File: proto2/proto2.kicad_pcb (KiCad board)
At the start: 2 copper layers, 187.5 x 109.8 mm, 182 parts, among them J1 Output 1, J10 Output, J11 Device, J12 Daughter Card, J2 Main Power, J3 Output, J4 Output, J5 Device, J6 Output, J7 Device, J8 Output, J9 Device, SW1 SW_DIP_x04, U1 AQY282SX, U10 AQY282SX, U11 AQY282SX, U12 AQY282SX, U13 LDO, U2 AQY282SX, U3 AQY282SX, U4 AQY282SX, U5 AQY282SX, U6 AQY282SX, U7 AQY282SX, U8 AQY282SX, U9 AQY282SX

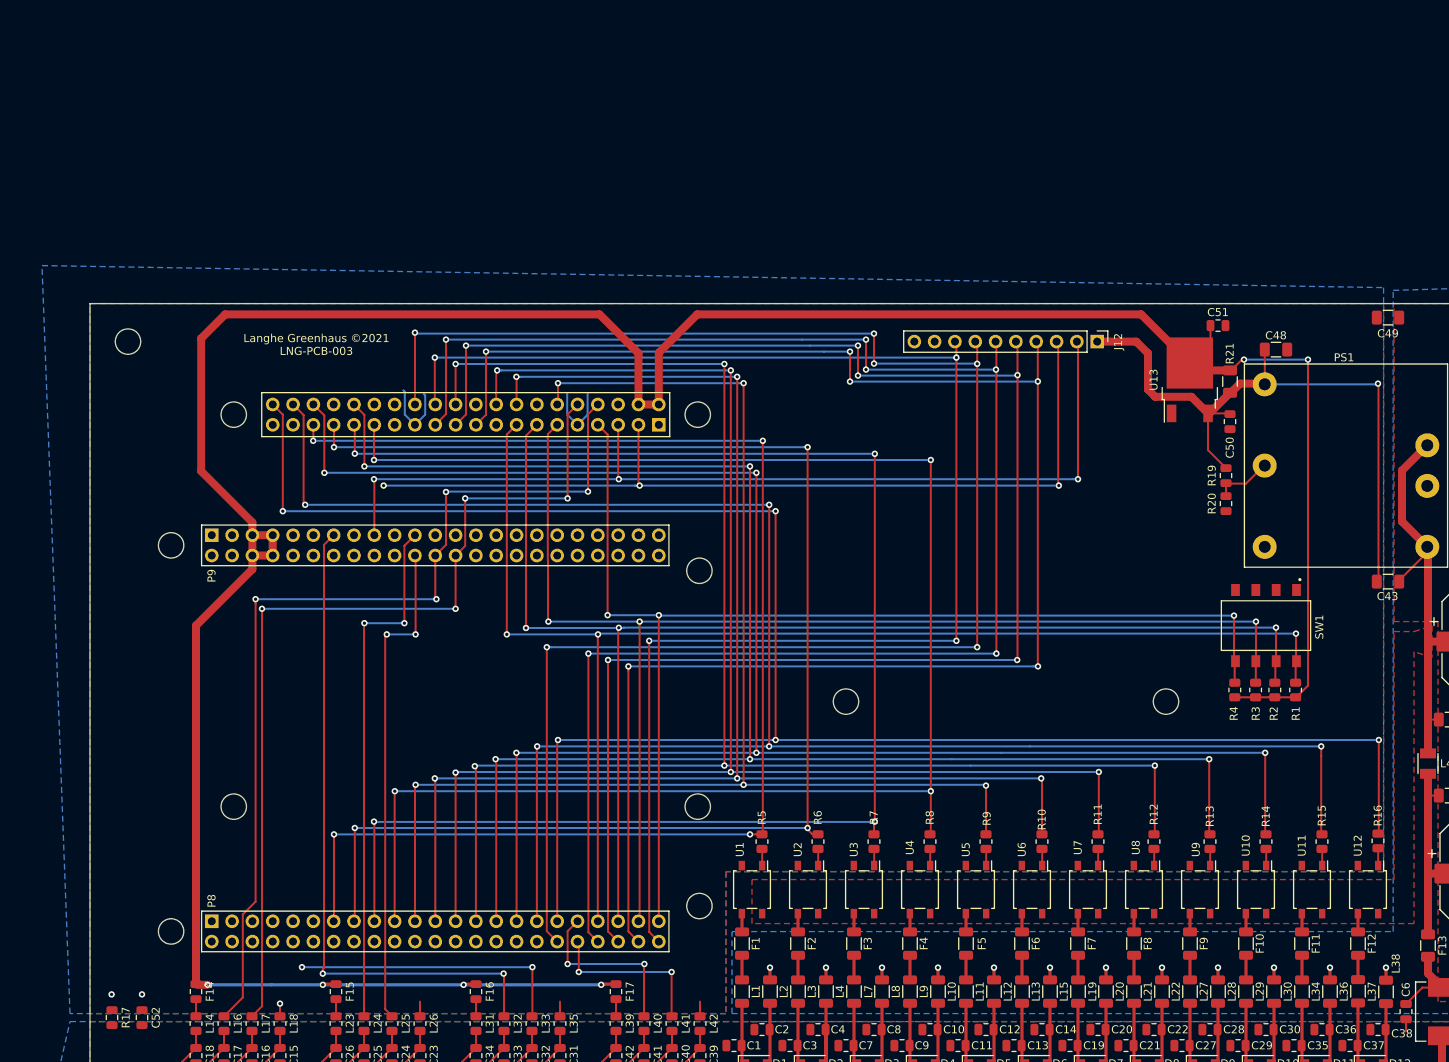
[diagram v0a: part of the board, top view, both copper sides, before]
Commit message: Added MOSFET drivers for the SSRs, pullups for I2C, and referenced DIP switches to 3V3.
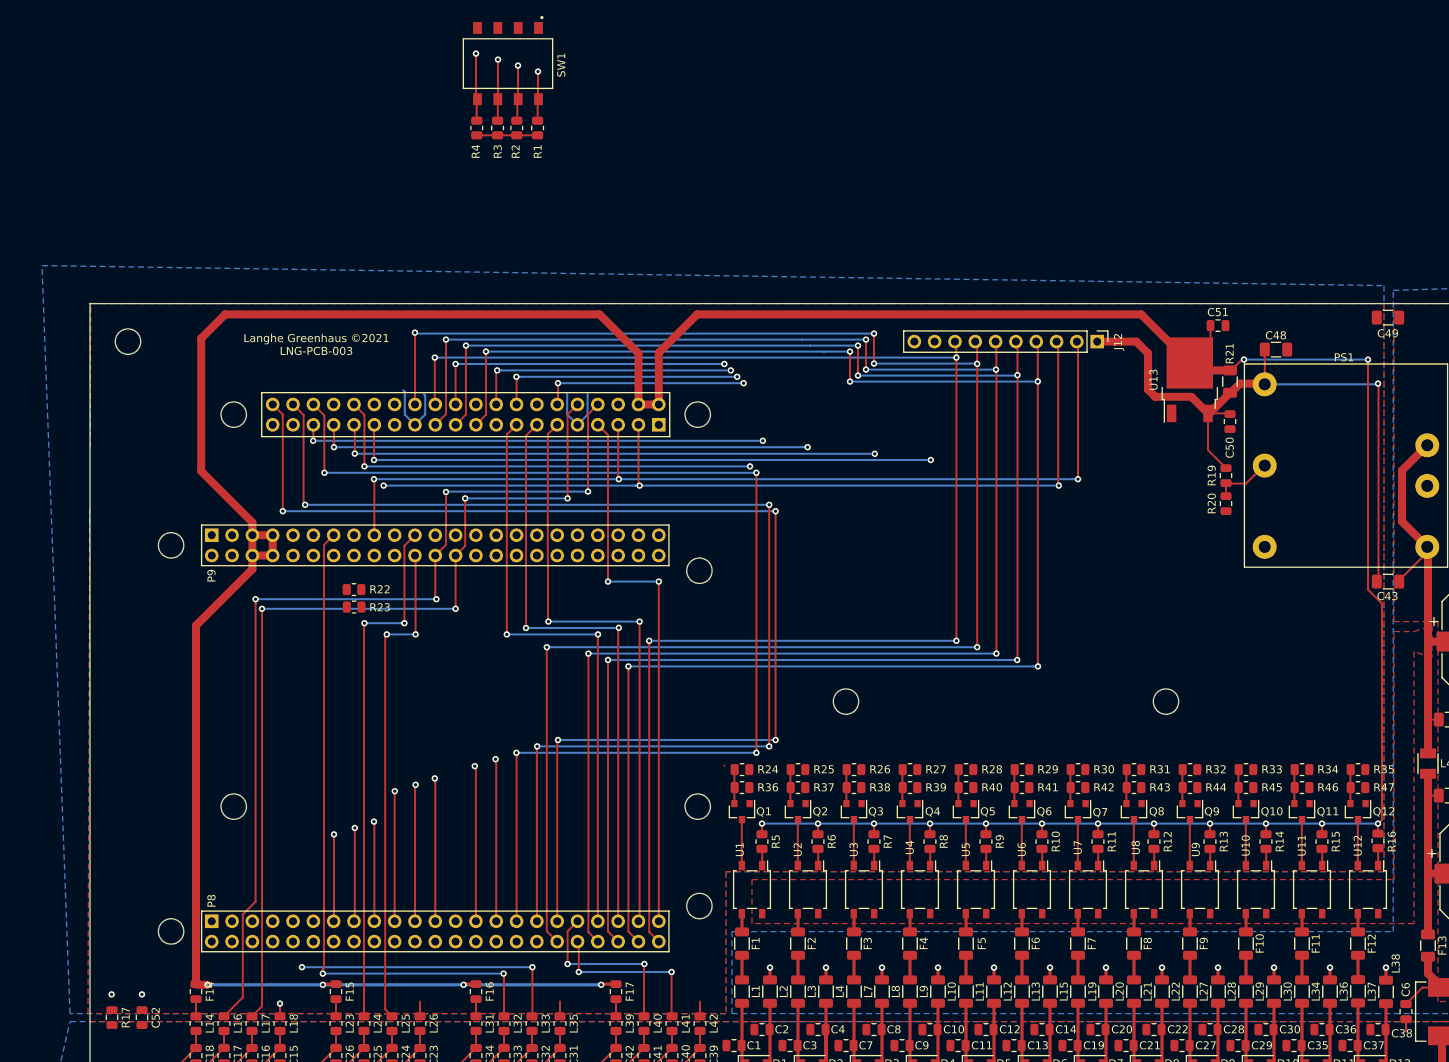
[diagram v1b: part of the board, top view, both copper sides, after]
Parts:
- added Q1: 2N7002, Package_TO_SOT_SMD:SOT-23, F.Cu at (112.0, 116.8)
- added Q10: 2N7002, Package_TO_SOT_SMD:SOT-23, F.Cu at (175.0, 116.8)
- added Q11: 2N7002, Package_TO_SOT_SMD:SOT-23, F.Cu at (182.0, 116.8)
- added Q12: 2N7002, Package_TO_SOT_SMD:SOT-23, F.Cu at (189.0, 116.8)
- added Q2: 2N7002, Package_TO_SOT_SMD:SOT-23, F.Cu at (119.0, 116.8)
- added Q3: 2N7002, Package_TO_SOT_SMD:SOT-23, F.Cu at (126.0, 116.8)
- added Q4: 2N7002, Package_TO_SOT_SMD:SOT-23, F.Cu at (133.0, 116.8)
- added Q5: 2N7002, Package_TO_SOT_SMD:SOT-23, F.Cu at (140.0, 116.8)
- added Q6: 2N7002, Package_TO_SOT_SMD:SOT-23, F.Cu at (147.0, 116.8)
- added Q7: 2N7002, Package_TO_SOT_SMD:SOT-23, F.Cu at (154.0, 116.8)
- added Q8: 2N7002, Package_TO_SOT_SMD:SOT-23, F.Cu at (161.0, 116.8)
- added Q9: 2N7002, Package_TO_SOT_SMD:SOT-23, F.Cu at (168.0, 116.8)
- added R22: 10K, Resistor_SMD:R_0805_2012Metric, F.Cu at (63.5, 89.0)
- added R23: 10K, Resistor_SMD:R_0805_2012Metric, F.Cu at (63.5, 91.2)
- added R24: 1K, Resistor_SMD:R_0805_2012Metric, F.Cu at (112.0, 111.5)
- added R25: 1K, Resistor_SMD:R_0805_2012Metric, F.Cu at (119.0, 111.5)
- added R26: 1K, Resistor_SMD:R_0805_2012Metric, F.Cu at (126.0, 111.5)
- added R27: 1K, Resistor_SMD:R_0805_2012Metric, F.Cu at (133.0, 111.5)
- added R28: 1K, Resistor_SMD:R_0805_2012Metric, F.Cu at (140.0, 111.5)
- added R29: 1K, Resistor_SMD:R_0805_2012Metric, F.Cu at (147.0, 111.5)
- added R30: 1K, Resistor_SMD:R_0805_2012Metric, F.Cu at (154.0, 111.5)
- added R31: 1K, Resistor_SMD:R_0805_2012Metric, F.Cu at (161.0, 111.5)
- added R32: 1K, Resistor_SMD:R_0805_2012Metric, F.Cu at (168.0, 111.5)
- added R33: 1K, Resistor_SMD:R_0805_2012Metric, F.Cu at (175.0, 111.5)
- added R34: 1K, Resistor_SMD:R_0805_2012Metric, F.Cu at (182.0, 111.5)
- added R35: 1K, Resistor_SMD:R_0805_2012Metric, F.Cu at (189.0, 111.5)
- added R36: 27K, Resistor_SMD:R_0805_2012Metric, F.Cu at (112.0, 113.8)
- added R37: 27K, Resistor_SMD:R_0805_2012Metric, F.Cu at (119.0, 113.8)
- added R38: 27K, Resistor_SMD:R_0805_2012Metric, F.Cu at (126.0, 113.8)
- added R39: 27K, Resistor_SMD:R_0805_2012Metric, F.Cu at (133.0, 113.8)
- added R40: 27K, Resistor_SMD:R_0805_2012Metric, F.Cu at (140.0, 113.8)
- added R41: 27K, Resistor_SMD:R_0805_2012Metric, F.Cu at (147.0, 113.8)
- added R42: 27K, Resistor_SMD:R_0805_2012Metric, F.Cu at (154.0, 113.8)
- added R43: 27K, Resistor_SMD:R_0805_2012Metric, F.Cu at (161.0, 113.8)
- added R44: 27K, Resistor_SMD:R_0805_2012Metric, F.Cu at (168.0, 113.8)
- added R45: 27K, Resistor_SMD:R_0805_2012Metric, F.Cu at (175.0, 113.8)
- added R46: 27K, Resistor_SMD:R_0805_2012Metric, F.Cu at (182.0, 113.8)
- added R47: 27K, Resistor_SMD:R_0805_2012Metric, F.Cu at (189.0, 113.8)
- moved R2 118.0 mm to (83.8, 31.3)
- moved R4 118.0 mm to (78.8, 31.3)
- moved SW1 118.0 mm to (82.8, 23.2)
- moved R1 118.0 mm to (86.5, 31.3)
- moved R3 118.0 mm to (81.5, 31.3)
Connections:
- F3 pad 1: DQ2_1 -> Net-(F3-Pad1)
- F4 pad 1: DQ2_2 -> Net-(F4-Pad1)
- R1 pad 1: +5V -> +3V3
- R10 pad 2: OUT_6 -> +5V
- R11 pad 2: OUT_7 -> +5V
- R12 pad 2: OUT_8 -> +5V
- R13 pad 2: OUT_9 -> +5V
- R14 pad 2: OUT_10 -> +5V
- R15 pad 2: OUT_11 -> +5V
- R16 pad 2: OUT_12 -> +5V
- R2 pad 1: +5V -> +3V3
- R3 pad 1: +5V -> +3V3
- R4 pad 1: +5V -> +3V3
- R5 pad 2: OUT_1 -> +5V
- R6 pad 2: OUT_2 -> +5V
- R7 pad 2: OUT_3 -> +5V
- R8 pad 2: OUT_4 -> +5V
- R9 pad 2: OUT_5 -> +5V
- U1 pad 2: GND -> Net-(Q1-Pad3)
- U10 pad 2: GND -> Net-(Q10-Pad3)
- U11 pad 2: GND -> Net-(Q11-Pad3)
- U12 pad 2: GND -> Net-(Q12-Pad3)
- U2 pad 2: GND -> Net-(Q2-Pad3)
- U3 pad 2: GND -> Net-(Q3-Pad3)
- U4 pad 2: GND -> Net-(Q4-Pad3)
- U5 pad 2: GND -> Net-(Q5-Pad3)
- U6 pad 2: GND -> Net-(Q6-Pad3)
- U7 pad 2: GND -> Net-(Q7-Pad3)
- U8 pad 2: GND -> Net-(Q8-Pad3)
- U9 pad 2: GND -> Net-(Q9-Pad3)
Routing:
- net OUT_7: track 190.6 -> 33.5 mm, vias 5 -> 2
- net OUT_8: track 202.0 -> 58.2 mm, vias 5 -> 3
- net OUT_9: track 212.0 -> 76.8 mm, vias 5 -> 3
- net OUT_6: track 182.0 -> 49.0 mm, vias 5 -> 3
- net OUT_5: track 170.6 -> 43.0 mm, vias 5 -> 3
- net OUT_4: track 204.1 -> 90.3 mm, vias 4 -> 3
- net OUT_3: track 191.3 -> 81.1 mm, vias 4 -> 3
- net +5V: track 369.2 -> 477.8 mm, vias 6 -> 18
- net OUT_2: track 179.6 -> 73.7 mm, vias 4 -> 3
- net OUT_1: track 172.5 -> 69.1 mm, vias 4 -> 3
- net BS_1: track 167.4 -> 80.2 mm
- net OUT_12: track 241.1 -> 154.0 mm, vias 5 -> 4
- net BS_2: track 163.5 -> 81.4 mm
- net OUT_11: track 232.3 -> 152.2 mm, vias 5 -> 4
- net BS_3: track 158.8 -> 81.8 mm
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
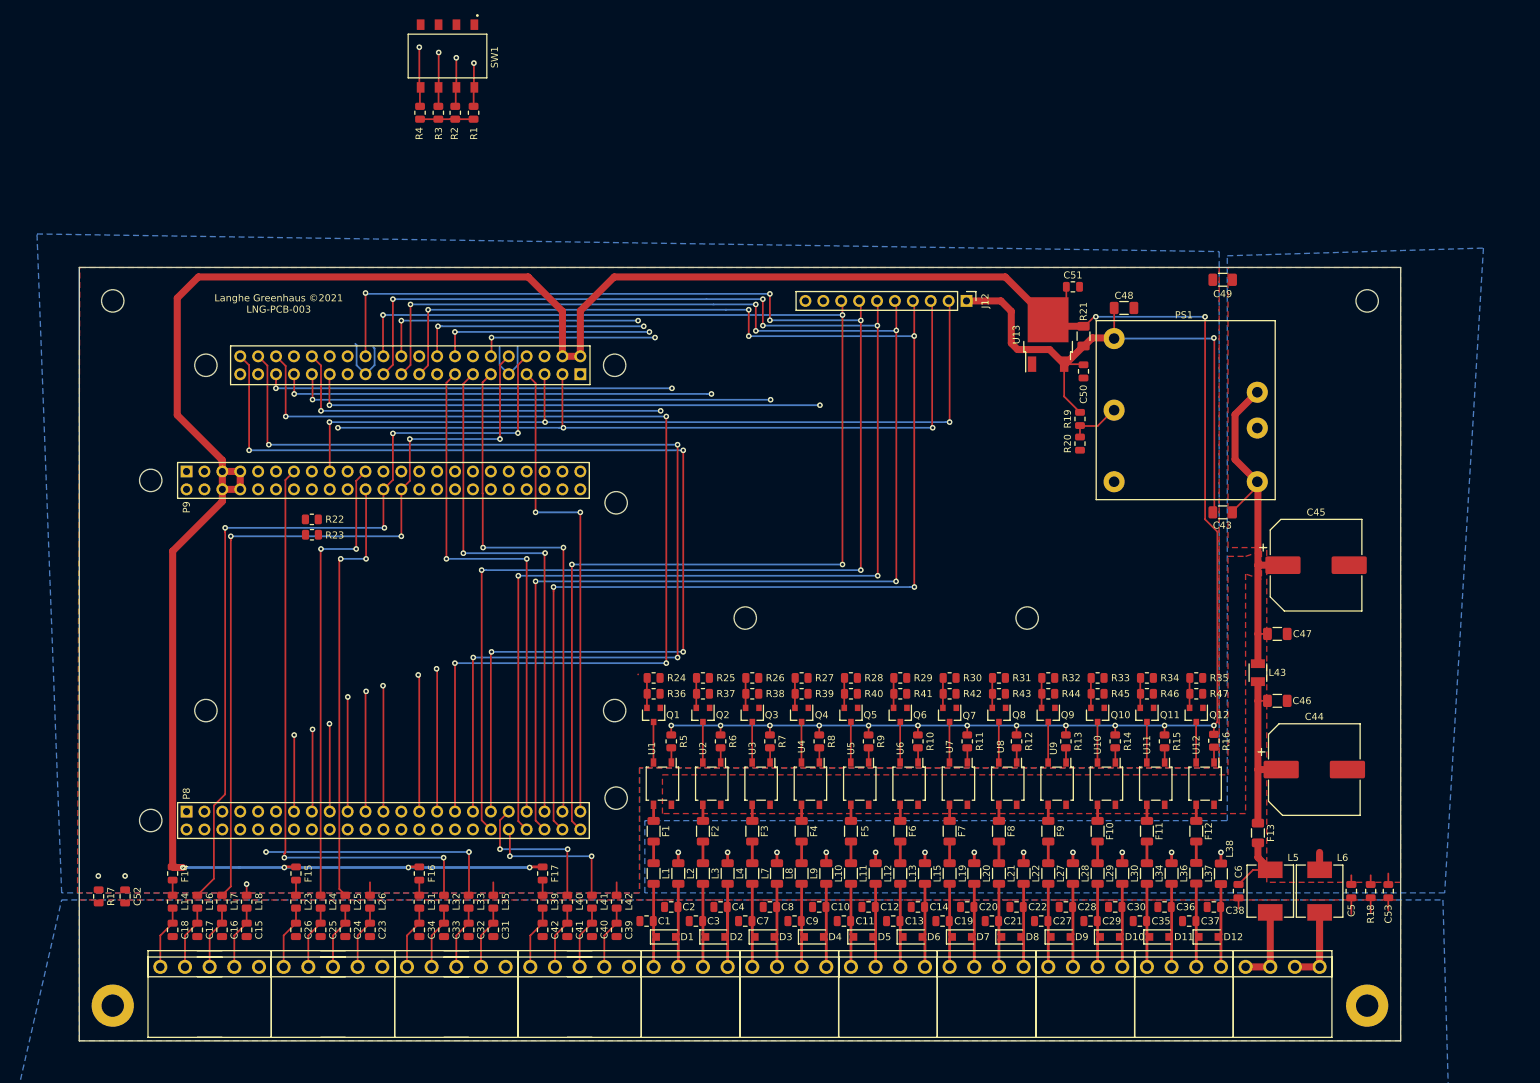
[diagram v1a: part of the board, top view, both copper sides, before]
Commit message: Removed Raspberry Pi, added spacing to terminals.
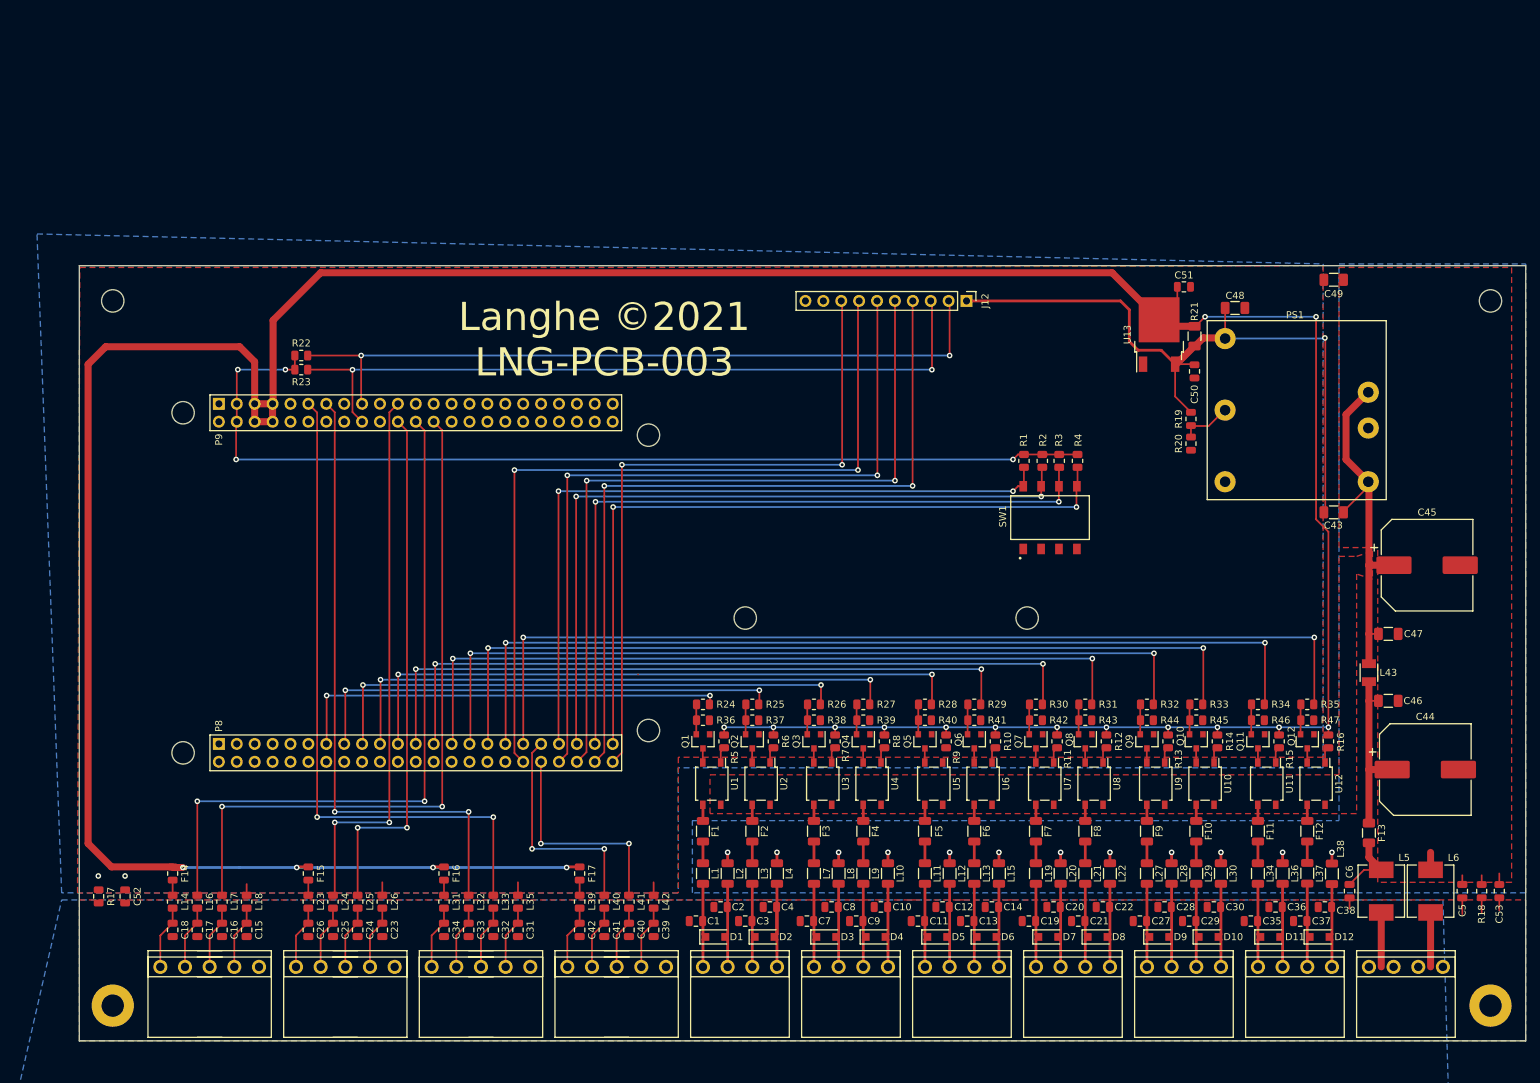
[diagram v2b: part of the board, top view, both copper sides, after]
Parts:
- removed RP1: RaspberryPi, BCR_SBC:RaspberryPi_UpsideDown
- moved SW1 107.7 mm to (168.2, 88.8), turned to 90 degrees
- moved R4 105.6 mm to (172.2, 80.7), turned to 270 degrees
- moved R3 101.0 mm to (169.6, 80.7), turned to 270 degrees
- moved R2 96.8 mm to (167.2, 80.7), turned to 270 degrees
- moved R1 92.4 mm to (164.6, 80.7), turned to 270 degrees
- moved R23 23.5 mm to (62.0, 67.8)
- moved R22 23.3 mm to (62.0, 65.8)
- moved J2 17.5 mm to (218.8, 152.5)
- moved MH3 17.5 mm to (230.8, 58.0)
- moved MH4 17.5 mm to (230.8, 158.0)
- moved R16 16.3 mm to (207.8, 120.5)
- moved R15 16.2 mm to (200.8, 120.5)
- moved Q11 16.2 mm to (197.8, 120.5)
- moved Q12 16.2 mm to (204.8, 120.5)
- moved R34 16.2 mm to (197.8, 115.2)
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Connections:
- F3 pad 1: Net-(F3-Pad1) -> DQ2_1
- F4 pad 1: Net-(F4-Pad1) -> DQ2_2
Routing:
- net +3V3: track 8.49 -> 143.5 mm, vias 0 -> 4
- net GP_3: track 210.3 -> 110.1 mm, vias 6 -> 2
- net GP_2: track 209.8 -> 110.0 mm, vias 6 -> 2
- net GP_1: track 209.1 -> 109.7 mm, vias 6 -> 2
- net GP_4: track 212.4 -> 114.9 mm, vias 6 -> 2
- net BS_5: track 185.0 -> 97.2 mm, vias 4 -> 2
- net OUT_7: track 33.5 -> 103.5 mm
- net RX_3: track 34.9 -> 95.3 mm
- net OUT_8: track 58.2 -> 109.5 mm, vias 3 -> 2
- net OUT_5: track 43.0 -> 89.9 mm, vias 3 -> 2
- net OUT_6: track 49.0 -> 95.9 mm, vias 3 -> 2
- net OUT_9: track 76.8 -> 117.2 mm, vias 3 -> 2
- net +5V: track 477.8 -> 509.5 mm
- net BS_4: track 77.6 -> 105.1 mm, vias 3 -> 2
- net OUT_10: track 149.2 -> 123.3 mm, vias 4 -> 2
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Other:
- board size 187.5 x 109.8 mm -> 205.2 x 110 mm
- board text added: "Langhe ©2021 LNG-PCB-003"
- board text removed: "Langhe Greenhaus ©2021 LNG-PCB-003"
